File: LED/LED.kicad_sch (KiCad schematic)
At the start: 22 parts, among them U1 ELD-426SYGWA, U10 ELD-426SYGWA, U11 ELD-426SYGWA, U12 ELD-426SYGWA, U13 DA04-11CGKWA, U14 DA04-11CGKWA, U15 DA04-11CGKWA, U16 DA04-11CGKWA, U17 DA04-11CGKWA, U18 DA04-11CGKWA, U19 DA04-11CGKWA, U2 ELD-426SYGWA, U20 DA04-11CGKWA, U21 DA04-11CGKWA, U22 DA04-11CGKWA, U3 ELD-426SYGWA, U4 ELD-426SYGWA, U5 ELD-426SYGWA, U6 ELD-426SYGWA, U7 ELD-426SYGWA, U8 ELD-426SYGWA, U9 ELD-426SYGWA

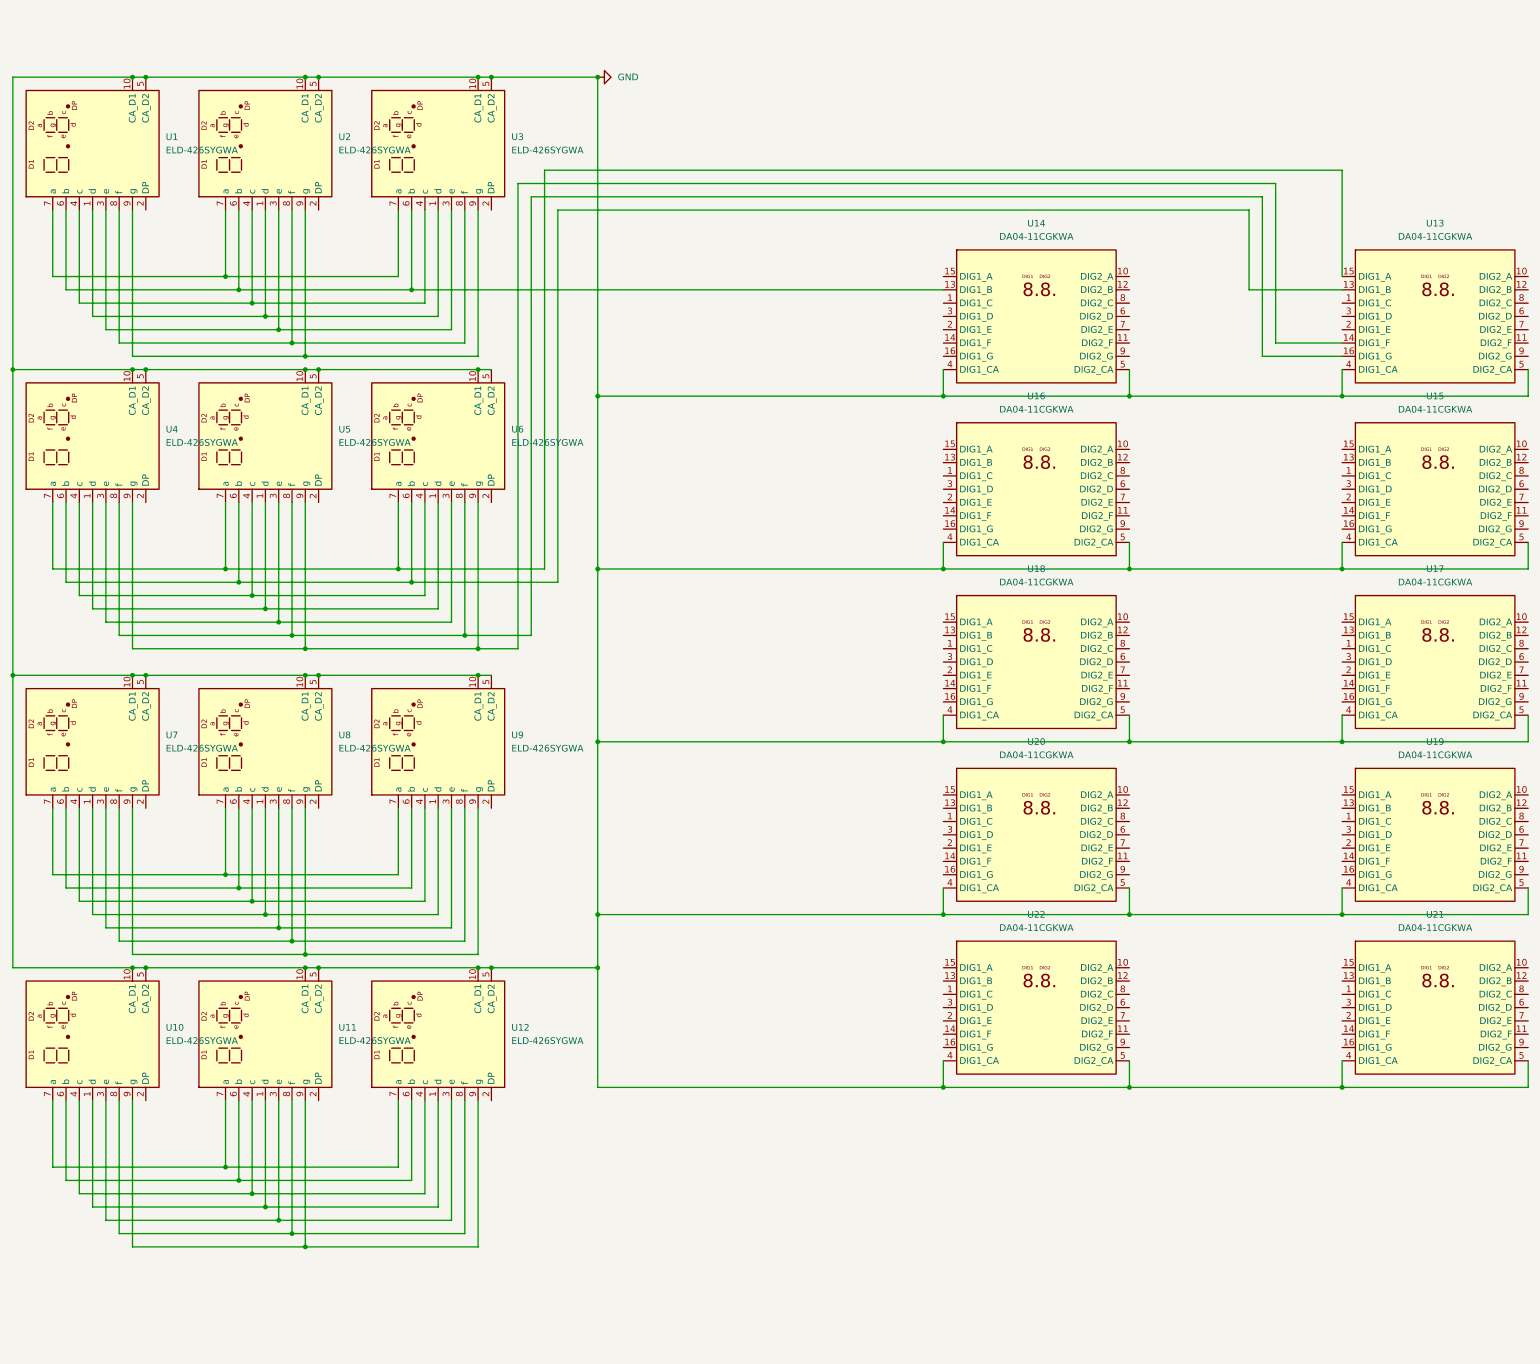
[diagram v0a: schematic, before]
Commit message: add led board
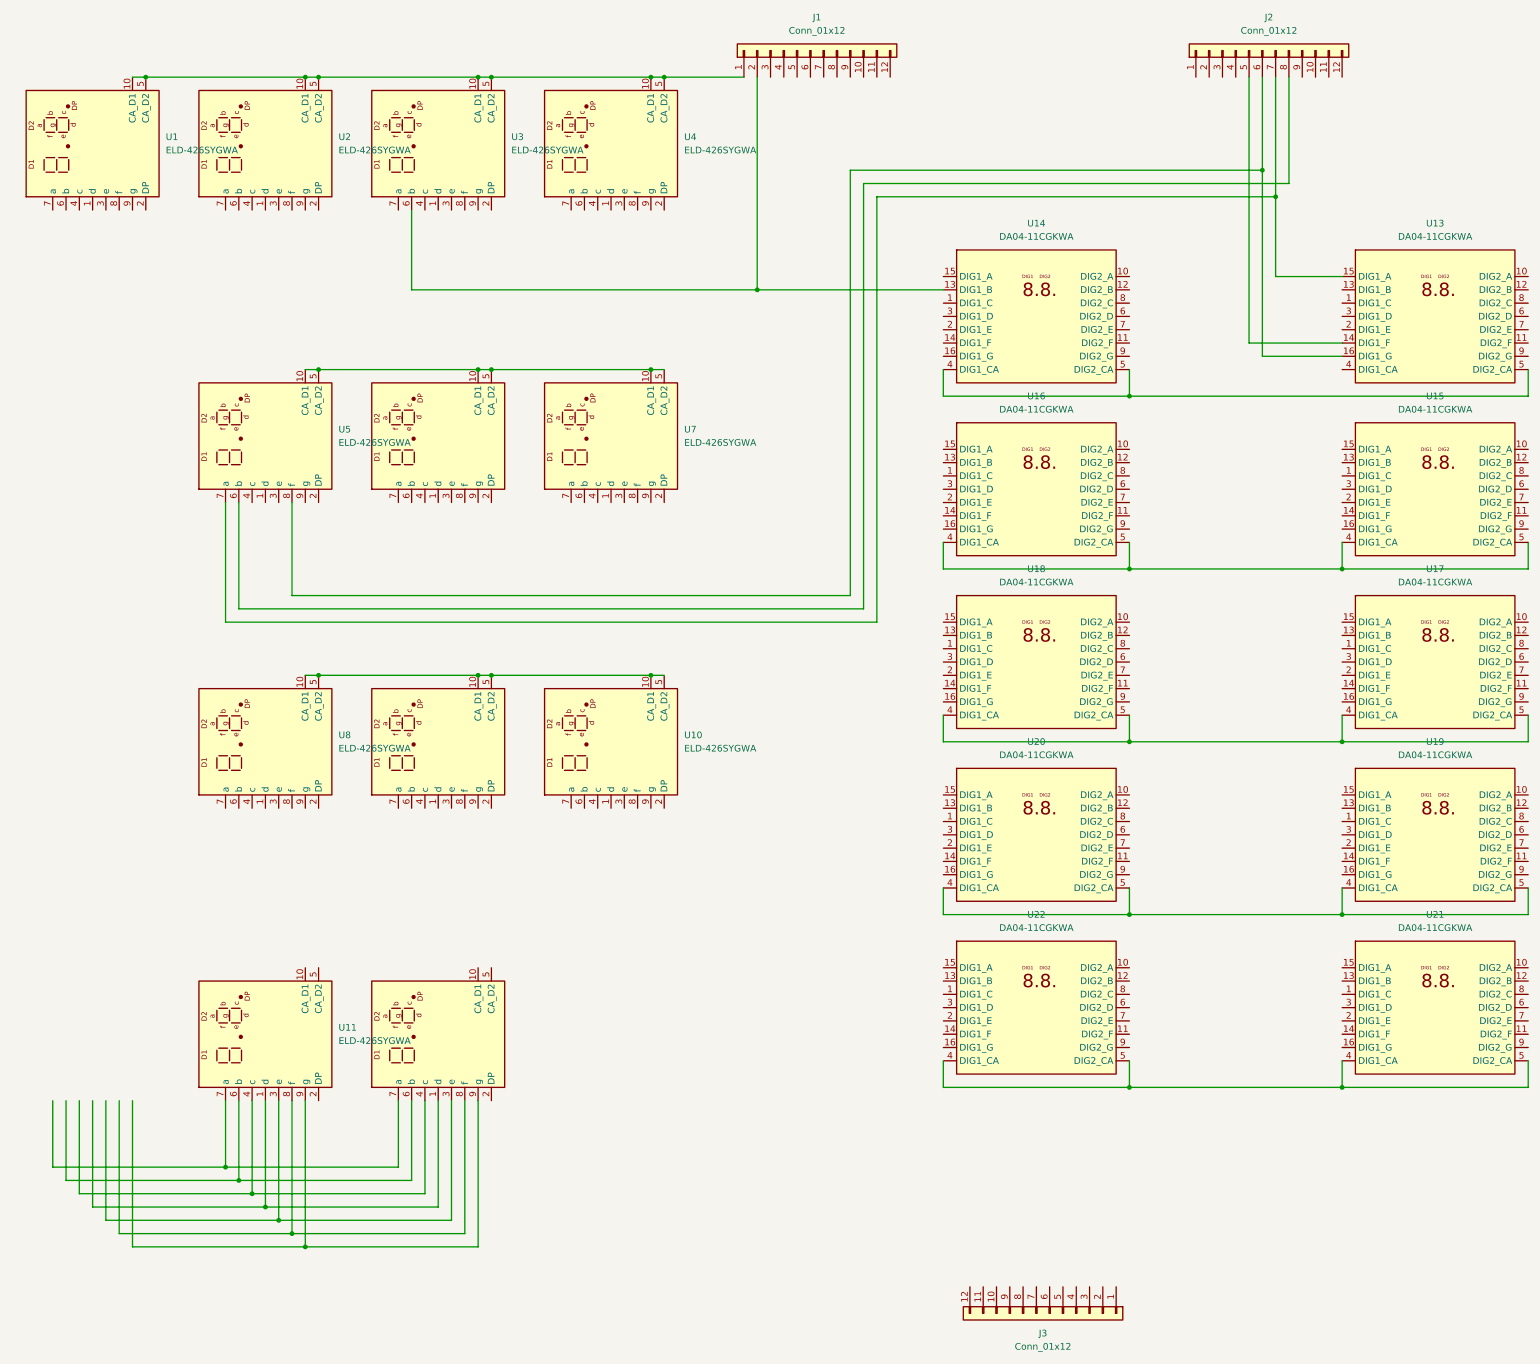
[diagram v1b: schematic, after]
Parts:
- added J1, J2, J3: Conn_01x12, ConnectorPad:Pad12, symbol Connector_Generic:Conn_01x12
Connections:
- net at U14.13 (DIG1_B), U3.6 (b): now also J1.2 (Pin_2); no longer U1.6 (b), U2.6 (b)
- net at U13.15 (DIG1_A), U5.7 (a): now also J2.7 (Pin_7); no longer U4.7 (a), U6.7 (a)
- net at U13.16 (DIG1_G), U5.8 (f): now also J2.6 (Pin_6); no longer U4.8 (f), U6.8 (f)
- net at U11.1 (d), U12.1 (d): no longer U10.1 (d)
- net at U11.3 (e), U12.3 (e): no longer U10.3 (e)
- net at U11.4 (c), U12.4 (c): no longer U10.4 (c)
- net at U11.6 (b), U12.6 (b): no longer U10.6 (b)
- net at U11.7 (a), U12.7 (a): no longer U10.7 (a)
- net at U11.8 (f), U12.8 (f): no longer U10.8 (f)
- net at U11.9 (g), U12.9 (g): no longer U10.9 (g)
- removed net GND: U1.10 (CA_D1), U1.5 (CA_D2), U10.10 (CA_D1), U10.5 (CA_D2), U11.10 (CA_D1), U11.5 (CA_D2), U12.10 (CA_D1), U12.5 (CA_D2), U13.4 (DIG1_CA), U13.5 (DIG2_CA), U14.4 (DIG1_CA), U14.5 (DIG2_CA), U15.4 (DIG1_CA), U15.5 (DIG2_CA), U16.4 (DIG1_CA), U16.5 (DIG2_CA), U17.4 (DIG1_CA), U17.5 (DIG2_CA), U18.4 (DIG1_CA), U18.5 (DIG2_CA), U19.4 (DIG1_CA), U19.5 (DIG2_CA), U2.10 (CA_D1), U2.5 (CA_D2), U20.4 (DIG1_CA), U20.5 (DIG2_CA), U21.4 (DIG1_CA), U21.5 (DIG2_CA), U22.4 (DIG1_CA), U22.5 (DIG2_CA), U3.10 (CA_D1), U3.5 (CA_D2), U4.10 (CA_D1), U4.5 (CA_D2), U5.10 (CA_D1), U5.5 (CA_D2), U6.10 (CA_D1), U6.5 (CA_D2), U7.10 (CA_D1), U7.5 (CA_D2), U8.10 (CA_D1), U8.5 (CA_D2), U9.10 (CA_D1), U9.5 (CA_D2)
- new net: U10.10 (CA_D1), U10.5 (CA_D2), U8.10 (CA_D1), U8.5 (CA_D2), U9.10 (CA_D1), U9.5 (CA_D2)
- new net: U5.10 (CA_D1), U5.5 (CA_D2), U6.10 (CA_D1), U6.5 (CA_D2), U7.10 (CA_D1), U7.5 (CA_D2)
- new net: J1.1 (Pin_1), U1.10 (CA_D1), U1.5 (CA_D2), U2.10 (CA_D1), U2.5 (CA_D2), U3.10 (CA_D1), U3.5 (CA_D2), U4.10 (CA_D1), U4.5 (CA_D2)
- new net: U19.4 (DIG1_CA), U19.5 (DIG2_CA), U20.4 (DIG1_CA), U20.5 (DIG2_CA)
- new net: U17.4 (DIG1_CA), U17.5 (DIG2_CA), U18.4 (DIG1_CA), U18.5 (DIG2_CA)
- new net: U21.4 (DIG1_CA), U21.5 (DIG2_CA), U22.4 (DIG1_CA), U22.5 (DIG2_CA)
- new net: J2.8 (Pin_8), U5.6 (b)
- new net: U13.5 (DIG2_CA), U14.4 (DIG1_CA), U14.5 (DIG2_CA)
- new net: J2.5 (Pin_5), U13.14 (DIG1_F)
- new net: U15.4 (DIG1_CA), U15.5 (DIG2_CA), U16.4 (DIG1_CA), U16.5 (DIG2_CA)
- now unconnected: U1.1 (d), U1.3 (e), U1.4 (c), U1.7 (a), U1.8 (f), U1.9 (g), U13.13 (DIG1_B), U2.1 (d), U2.3 (e), U2.4 (c), U2.7 (a), U2.8 (f), U2.9 (g), U3.1 (d), U3.3 (e), U3.4 (c), U3.7 (a), U3.8 (f), U3.9 (g), U4.1 (d), U4.3 (e), U4.4 (c), U4.6 (b), U4.9 (g), U5.1 (d), U5.3 (e), U5.4 (c), U5.9 (g), U6.1 (d), U6.3 (e), U6.4 (c), U6.6 (b), U6.9 (g), U7.1 (d), U7.3 (e), U7.4 (c), U7.6 (b), U7.7 (a), U7.8 (f), U7.9 (g), U8.1 (d), U8.3 (e), U8.4 (c), U8.6 (b), U8.7 (a), U8.8 (f), U8.9 (g), U9.1 (d), U9.3 (e), U9.4 (c), U9.6 (b), U9.7 (a), U9.8 (f), U9.9 (g)
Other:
- moved on the sheet: U10, U4, U7
